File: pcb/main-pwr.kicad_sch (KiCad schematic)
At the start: 18 parts, among them U2 ADP5054

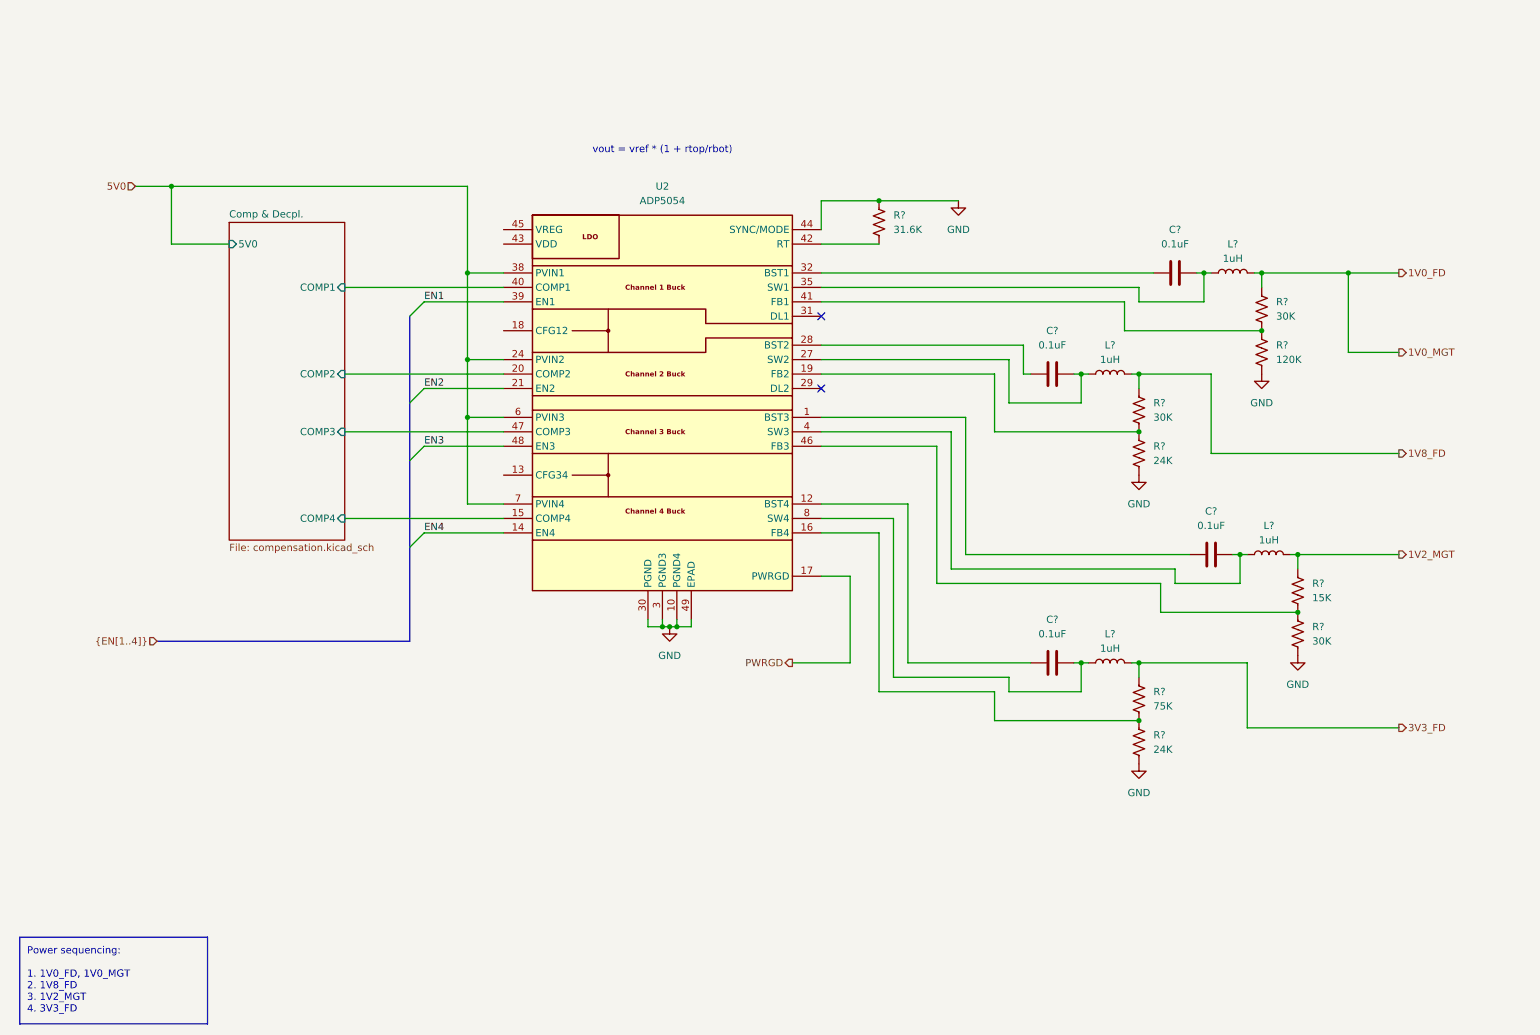
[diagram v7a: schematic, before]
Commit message: hierarchical current sense
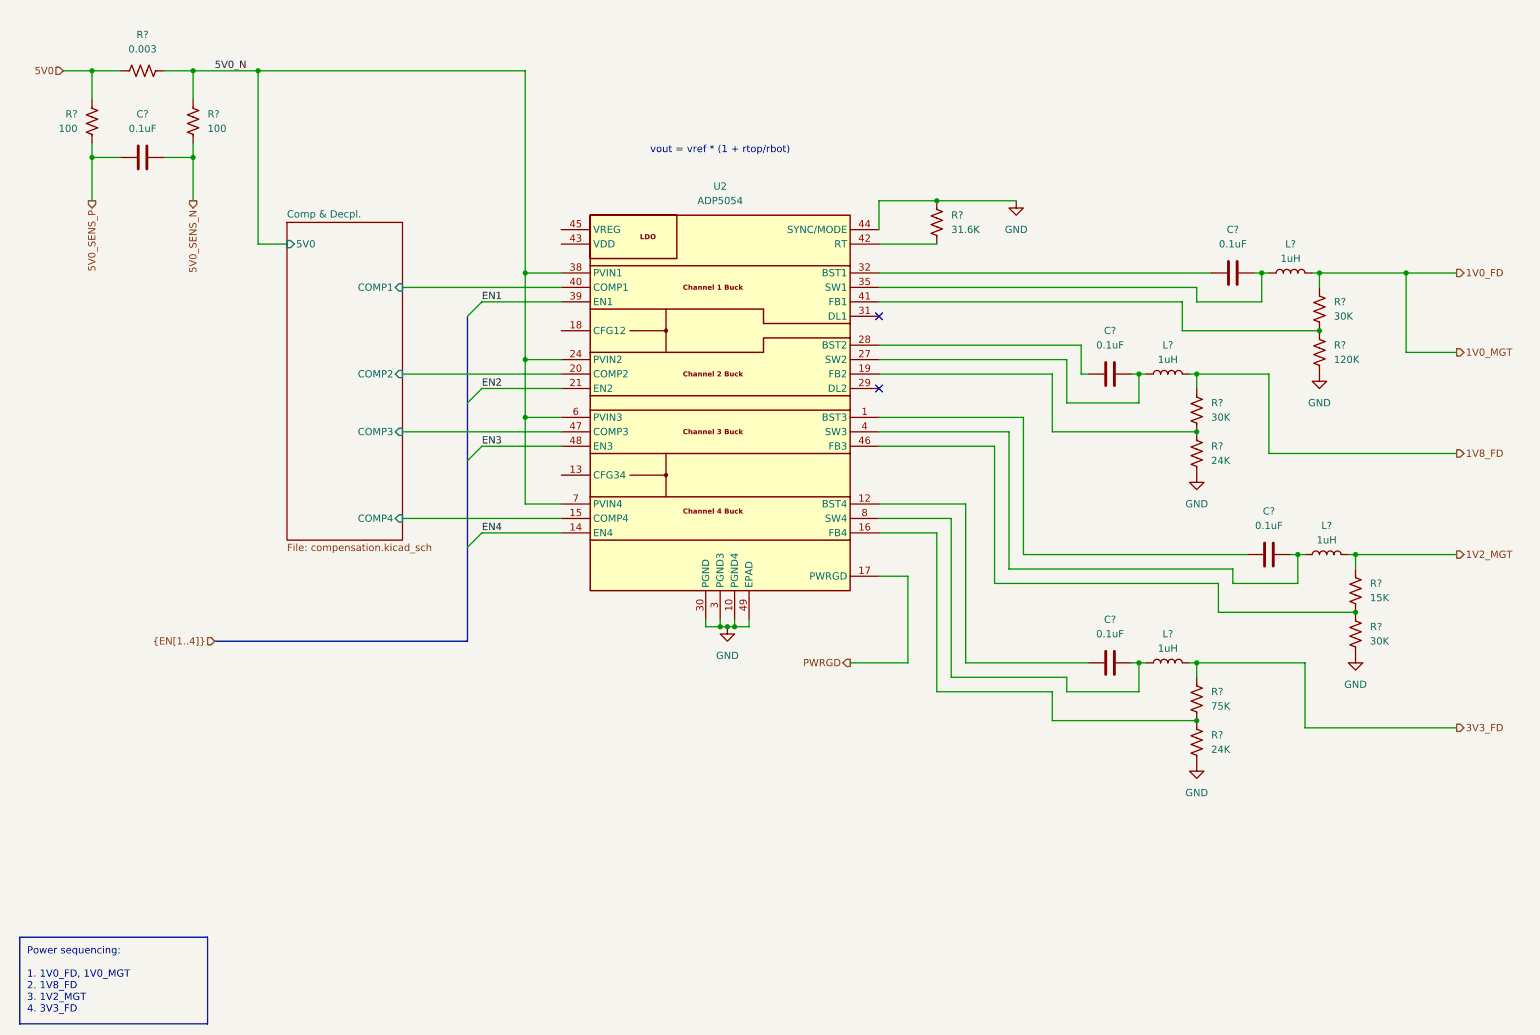
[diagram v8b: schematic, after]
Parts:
- added C?: 0.1uF, symbol Device:C
- added R?: 0.003, symbol Device:R_US
- added R? (x2): 100, symbol Device:R_US
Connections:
- net 5V0: now also R?.1, R?.2; no longer U2.22 (PVIN2), U2.23 (PVIN2), U2.24 (PVIN2), U2.36 (PVIN1), U2.37 (PVIN1), U2.38 (PVIN1), U2.6 (PVIN3), U2.7 (PVIN4)
- new net 5V0_N: R?.2, R?.2, U2.22 (PVIN2), U2.23 (PVIN2), U2.24 (PVIN2), U2.36 (PVIN1), U2.37 (PVIN1), U2.38 (PVIN1), U2.6 (PVIN3), U2.7 (PVIN4)
- new net 5V0_SENS_N: C?.2, R?.1
- new net 5V0_SENS_P: C?.1, R?.1
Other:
- moved on the sheet: C?, L?, R?, U2
